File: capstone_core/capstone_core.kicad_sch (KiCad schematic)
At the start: 6 parts, among them J1 Conn_01x02_Socket, J2 Conn_01x02_Socket, J3 Conn_01x10_Socket, J4 Conn_01x10_Socket, J5 Conn_02x20_Counter_Clockwise, J6 Conn_01x02_Socket

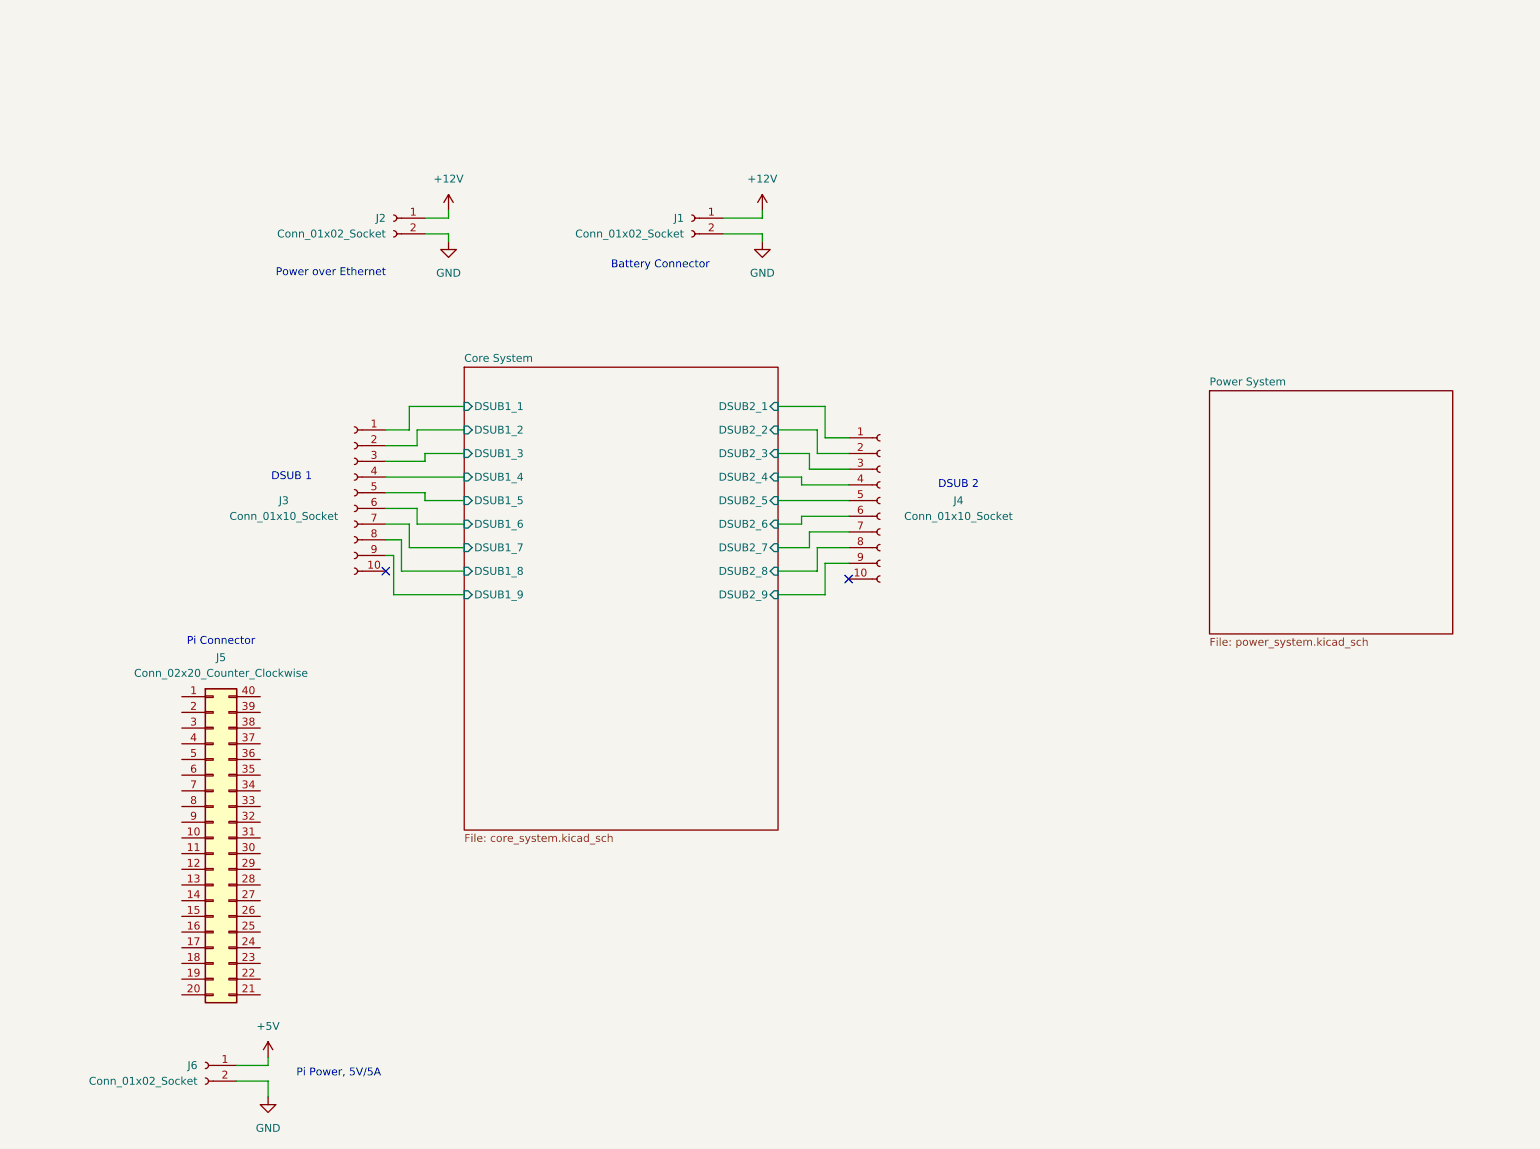
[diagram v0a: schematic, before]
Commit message: adding connectors, components, and footprints
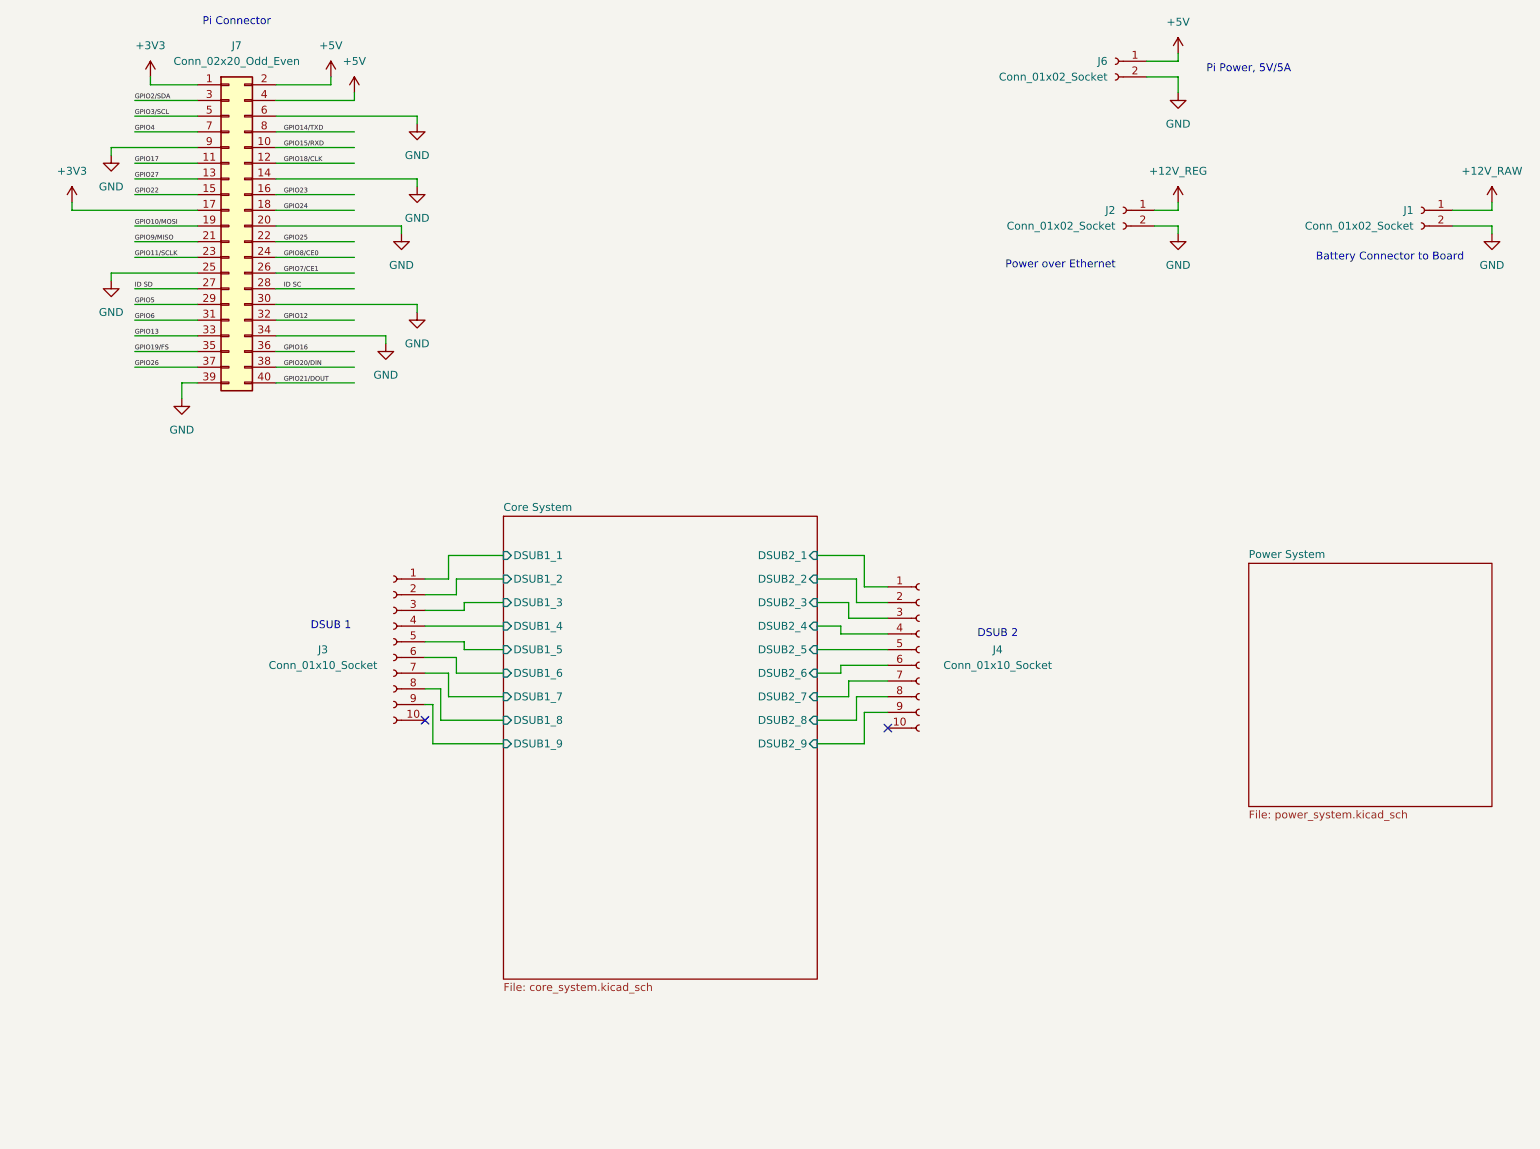
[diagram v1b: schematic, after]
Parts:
- removed J5: Conn_02x20_Counter_Clockwise, symbol Connector_Generic:Conn_02x20_Counter_Clockwise
- added J7: Conn_02x20_Odd_Even, Capstone Footprints:2x20_CONN_3020-40-0100-00_CNC, symbol Connector_Generic:Conn_02x20_Odd_Even
- J1, J2, J6: footprint (none) -> Capstone Footprints:1x2_CONN_SD-43650-010_02_MOL
- J3, J4: footprint Capstone Footprints:CON10_P100X100-RIBBON_TYC -> Capstone Footprints:2x5_CON10_P100X100-RIBBON_TYC
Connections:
- net +5V: now also J7.2 (Pin_2), J7.4 (Pin_4)
- net GND: now also J7.14 (Pin_14), J7.20 (Pin_20), J7.25 (Pin_25), J7.30 (Pin_30), J7.34 (Pin_34), J7.39 (Pin_39), J7.6 (Pin_6), J7.9 (Pin_9)
- net +12V renamed +12V_RAW
- net +12V_RAW: no longer J2.1 (Pin_1)
- new net +12V_REG: J2.1 (Pin_1)
- new net +3V3: J7.1 (Pin_1), J7.17 (Pin_17)
- new net GPIO10/MOSI: J7.19 (Pin_19)
- new net GPIO11/SCLK: J7.23 (Pin_23)
- new net GPIO12: J7.32 (Pin_32)
- new net GPIO13: J7.33 (Pin_33)
- new net GPIO14/TXD: J7.8 (Pin_8)
- new net GPIO15/RXD: J7.10 (Pin_10)
- new net GPIO16: J7.36 (Pin_36)
- new net GPIO17: J7.11 (Pin_11)
- new net GPIO18/CLK: J7.12 (Pin_12)
- new net GPIO19/FS: J7.35 (Pin_35)
- new net GPIO20/DIN: J7.38 (Pin_38)
- new net GPIO21/DOUT: J7.40 (Pin_40)
- new net GPIO22: J7.15 (Pin_15)
- new net GPIO23: J7.16 (Pin_16)
- new net GPIO24: J7.18 (Pin_18)
- new net GPIO25: J7.22 (Pin_22)
- new net GPIO26: J7.37 (Pin_37)
- new net GPIO27: J7.13 (Pin_13)
- new net GPIO2/SDA: J7.3 (Pin_3)
- new net GPIO3/SCL: J7.5 (Pin_5)
- new net GPIO4: J7.7 (Pin_7)
- new net GPIO5: J7.29 (Pin_29)
- new net GPIO6: J7.31 (Pin_31)
- new net GPIO7/CE1: J7.26 (Pin_26)
- new net GPIO8/CE0: J7.24 (Pin_24)
- new net GPIO9/MISO: J7.21 (Pin_21)
- new net ID SC: J7.28 (Pin_28)
- new net ID SD: J7.27 (Pin_27)
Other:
- note added: "Battery Connector to Board"
- note removed: "Battery Connector"
- moved on the sheet: J1, J2, J3, J4, J6

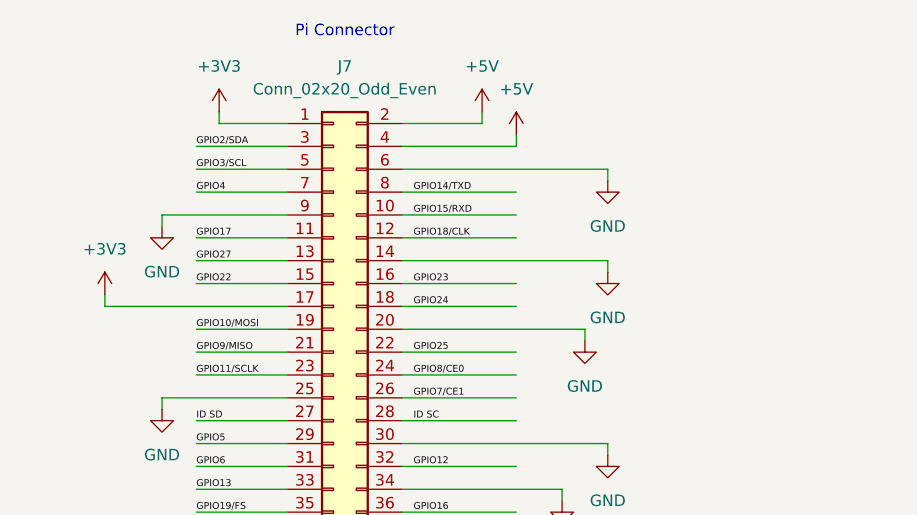
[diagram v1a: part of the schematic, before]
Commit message: Add ZED-F9P & level shifter
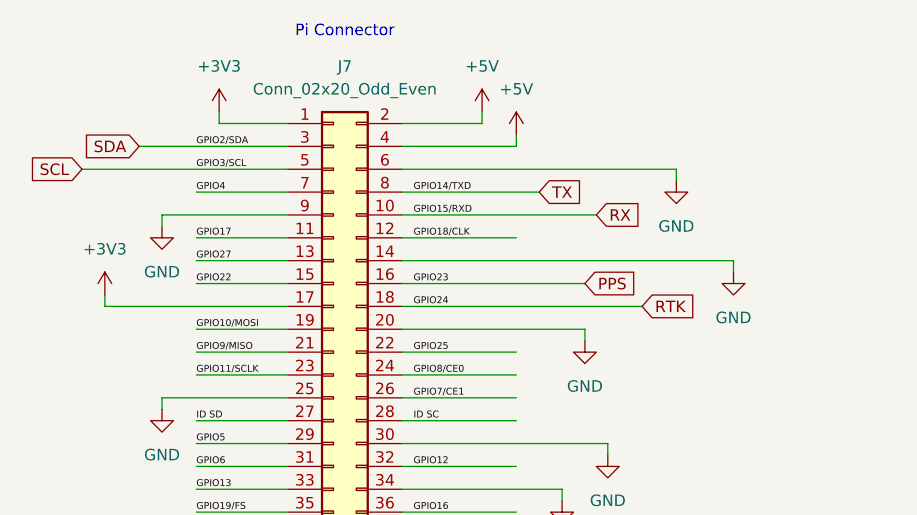
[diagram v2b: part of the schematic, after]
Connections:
- net GPIO14/TXD renamed TX
- net GPIO15/RXD renamed RX
- net GPIO23 renamed PPS
- net GPIO24 renamed RTK
- net GPIO2/SDA renamed SDA
- net GPIO3/SCL renamed SCL
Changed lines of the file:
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@@
-	(wire
-		(pts
-			(xy 34.29 31.75) (xy 44.45 31.75)
-		)
-		(stroke
-			(width 0)
-			(type default)
-		)
-	)
 	(wire
 		(pts
@@
 	(wire
 		(pts
-			(xy 57.15 49.53) (xy 69.85 49.53)
+			(xy 57.15 49.53) (xy 83.82 49.53)
 		)
 		(stroke
@@
 	(wire
 		(pts
-			(xy 57.15 39.37) (xy 69.85 39.37)
+			(xy 57.15 39.37) (xy 78.74 39.37)
 		)
 		(stroke
@@
 	(wire
 		(pts
-			(xy 57.15 36.83) (xy 69.85 36.83)
+			(xy 57.15 36.83) (xy 72.39 36.83)
 		)
 		(stroke
@@
 	(wire
 		(pts
+			(xy 27.94 31.75) (xy 44.45 31.75)
+		)
+		(stroke
+			(width 0)
+			(type default)
+		)
+	)
+	(wire
+		(pts
 			(xy 34.29 46.99) (xy 44.45 46.99)
 		)
@@
 	(wire
 		(pts
-			(xy 57.15 46.99) (xy 69.85 46.99)
+			(xy 57.15 46.99) (xy 77.47 46.99)
 		)
 		(stroke
@@
 	(wire
 		(pts
-			(xy 34.29 34.29) (xy 44.45 34.29)
-		)
-		(stroke
-			(width 0)
-			(type default)
-		)
-	)
-	(wire
-		(pts
 			(xy 81.28 119.38) (xy 87.63 119.38)
 		)
@@
 	(wire
 		(pts
-			(xy 80.01 44.45) (xy 80.01 45.72)
+			(xy 93.98 44.45) (xy 93.98 45.72)
 		)
 		(stroke
@@
 	(wire
 		(pts
-			(xy 57.15 44.45) (xy 80.01 44.45)
+			(xy 57.15 44.45) (xy 93.98 44.45)
 		)
 		(stroke
@@
 	(wire
 		(pts
-			(xy 80.01 34.29) (xy 80.01 35.56)
+			(xy 87.63 34.29) (xy 87.63 35.56)
 		)
 		(stroke
@@
 	(wire
 		(pts
+			(xy 21.59 34.29) (xy 44.45 34.29)
+		)
+		(stroke
+			(width 0)
+			(type default)
+		)
+	)
+	(wire
+		(pts
 			(xy 203.2 24.13) (xy 203.2 25.4)
 		)
@@
 	(wire
 		(pts
-			(xy 57.15 34.29) (xy 80.01 34.29)
+			(xy 57.15 34.29) (xy 87.63 34.29)
 		)
 		(stroke
@@
 			)
 			(justify left bottom)
+		)
+	)
+	(global_label "SCL"
+		(shape input)
+		(at 21.59 34.29 180)
+		(fields_autoplaced yes)
+		(effects
+			(font
+				(size 1.27 1.27)
+			)
+			(justify right)
+		)
+		(property "Intersheetrefs" "${INTERSHEET_REFS}"
+			(at 15.0972 34.29 0)
+			(effects
+				(font
+					(size 1.27 1.27)
+				)
+				(justify right)
+				(hide yes)
+			)
+		)
+	)
+	(global_label "TX"
+		(shape input)
+		(at 72.39 36.83 0)
+		(fields_autoplaced yes)
+		(effects
+			(font
+				(size 1.27 1.27)
+			)
+			(justify left)
+		)
+		(property "Intersheetrefs" "${INTERSHEET_REFS}"
+			(at 77.5523 36.83 0)
+			(effects
+				(font
+					(size 1.27 1.27)
+				)
+				(justify left)
+				(hide yes)
+			)
+		)
+	)
+	(global_label "RX"
+		(shape input)
+		(at 78.74 39.37 0)
+		(fields_autoplaced yes)
+		(effects
+			(font
+				(size 1.27 1.27)
+			)
+			(justify left)
+		)
+		(property "Intersheetrefs" "${INTERSHEET_REFS}"
+			(at 84.2047 39.37 0)
+			(effects
+				(font
+					(size 1.27 1.27)
+				)
+				(justify left)
+				(hide yes)
+			)
+		)
+	)
+	(global_label "PPS"
+		(shape input)
+		(at 77.47 46.99 0)
+		(fields_autoplaced yes)
+		(effects
+			(font
+				(size 1.27 1.27)
+			)
+			(justify left)
+		)
+		(property "Intersheetrefs" "${INTERSHEET_REFS}"
+			(at 84.2047 46.99 0)
+			(effects
+				(font
+					(size 1.27 1.27)
+				)
+				(justify left)
+				(hide yes)
+			)
+		)
+	)
+	(global_label "RTK"
+		(shape input)
+		(at 83.82 49.53 0)
+		(fields_autoplaced yes)
+		(effects
+			(font
+				(size 1.27 1.27)
+			)
+			(justify left)
+		)
+		(property "Intersheetrefs" "${INTERSHEET_REFS}"
+			(at 90.3128 49.53 0)
+			(effects
+				(font
+					(size 1.27 1.27)
+				)
+				(justify left)
+				(hide yes)
+			)
+		)
+	)
+	(global_label "SDA"
+		(shape input)
+		(at 27.94 31.75 180)
+		(fields_autoplaced yes)
+		(effects
+			(font
+				(size 1.27 1.27)
+			)
+			(justify right)
+		)
+		(property "Intersheetrefs" "${INTERSHEET_REFS}"
+			(at 21.3867 31.75 0)
+			(effects
+				(font
+					(size 1.27 1.27)
+				)
+				(justify right)
+				(hide yes)
+			)
 		)
 	)
@@
 	(symbol
 		(lib_id "power:GND")
-		(at 80.01 45.72 0)
+		(at 93.98 45.72 0)
 		(unit 1)
 		(exclude_from_sim no)
@@
 		(fields_autoplaced yes)
 		(property "Reference" "#PWR016"
-			(at 80.01 52.07 0)
+			(at 93.98 52.07 0)
 			(effects
 				(font
@@
 		)
 		(property "Value" "GND"
-			(at 80.01 50.8 0)
+			(at 93.98 50.8 0)
 			(effects
 				(font
@@
 		)
 		(property "Footprint" ""
-			(at 80.01 45.72 0)
+			(at 93.98 45.72 0)
 			(effects
 				(font
@@
 		)
 		(property "Datasheet" ""
-			(at 80.01 45.72 0)
+			(at 93.98 45.72 0)
 			(effects
 				(font
@@
 		)
 		(property "Description" "Power symbol creates a global label with name \"GND\" , ground"
-			(at 80.01 45.72 0)
+			(at 93.98 45.72 0)
 			(effects
 				(font
@@
 	(symbol
 		(lib_id "power:GND")
-		(at 80.01 35.56 0)
+		(at 87.63 35.56 0)
 		(unit 1)
 		(exclude_from_sim no)
@@
 		(fields_autoplaced yes)
 		(property "Reference" "#PWR011"
-			(at 80.01 41.91 0)
+			(at 87.63 41.91 0)
 			(effects
 				(font
@@
 		)
 		(property "Value" "GND"
-			(at 80.01 40.64 0)
+			(at 87.63 40.64 0)
 			(effects
 				(font
@@
 		)
 		(property "Footprint" ""
-			(at 80.01 35.56 0)
+			(at 87.63 35.56 0)
 			(effects
 				(font
@@
 		)
 		(property "Datasheet" ""
-			(at 80.01 35.56 0)
+			(at 87.63 35.56 0)
 			(effects
 				(font
@@
 		)
 		(property "Description" "Power symbol creates a global label with name \"GND\" , ground"
-			(at 80.01 35.56 0)
-			(effects
-				(font
+			(at 87.63 35.56 0)
+			(effects
+				(font
